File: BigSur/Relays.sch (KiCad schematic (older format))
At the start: 3 parts, among them K1 G5LE-1A-VDDC12, Q3 Q_NPN_BCE

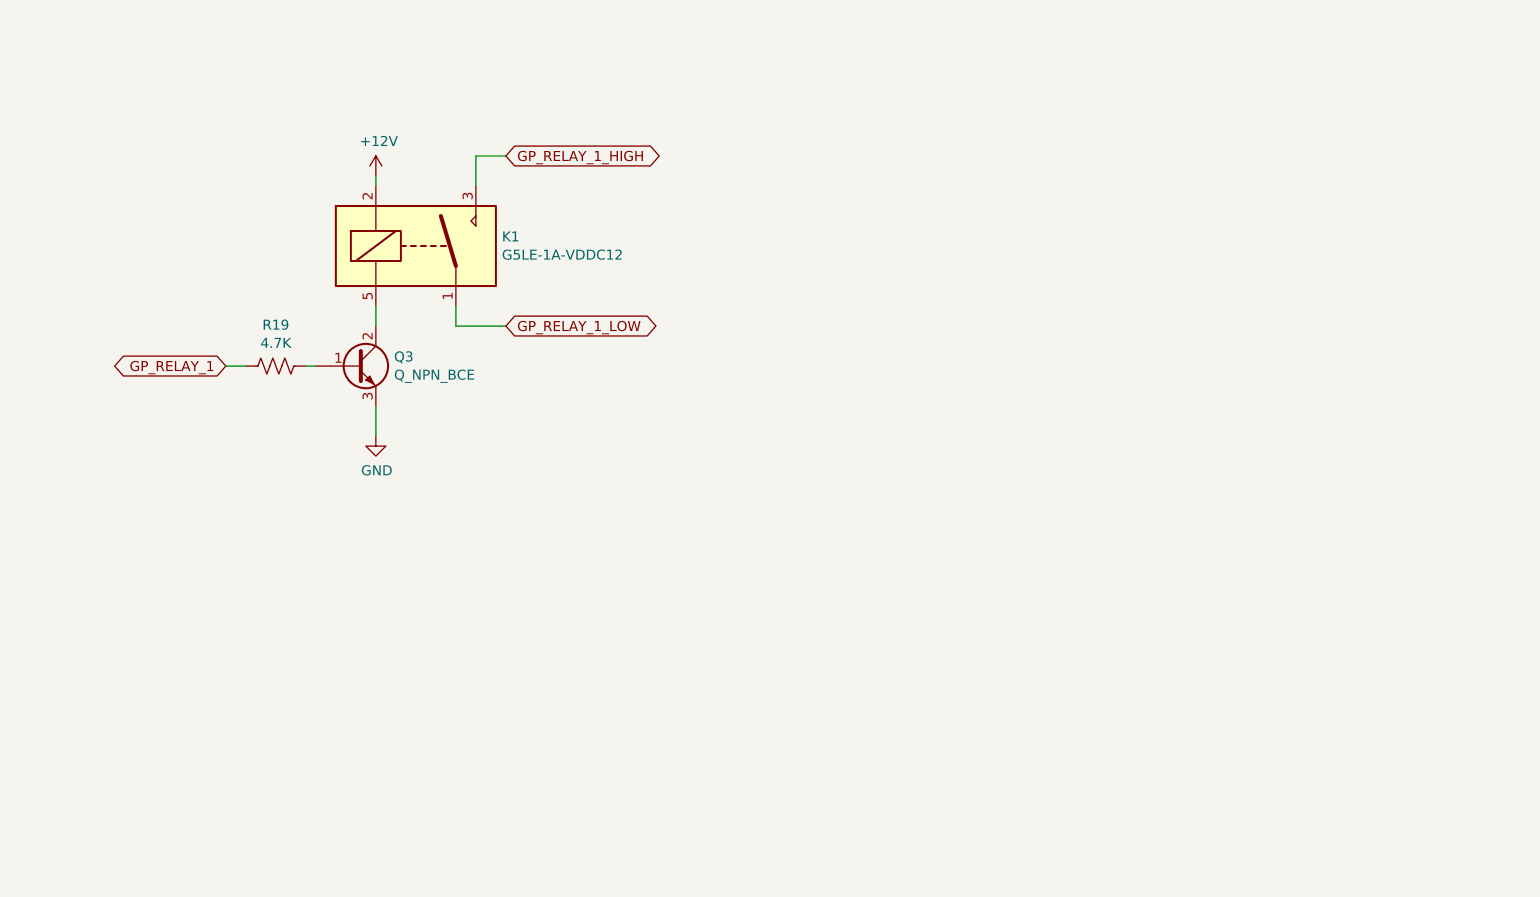
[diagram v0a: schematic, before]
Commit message: Updated test points
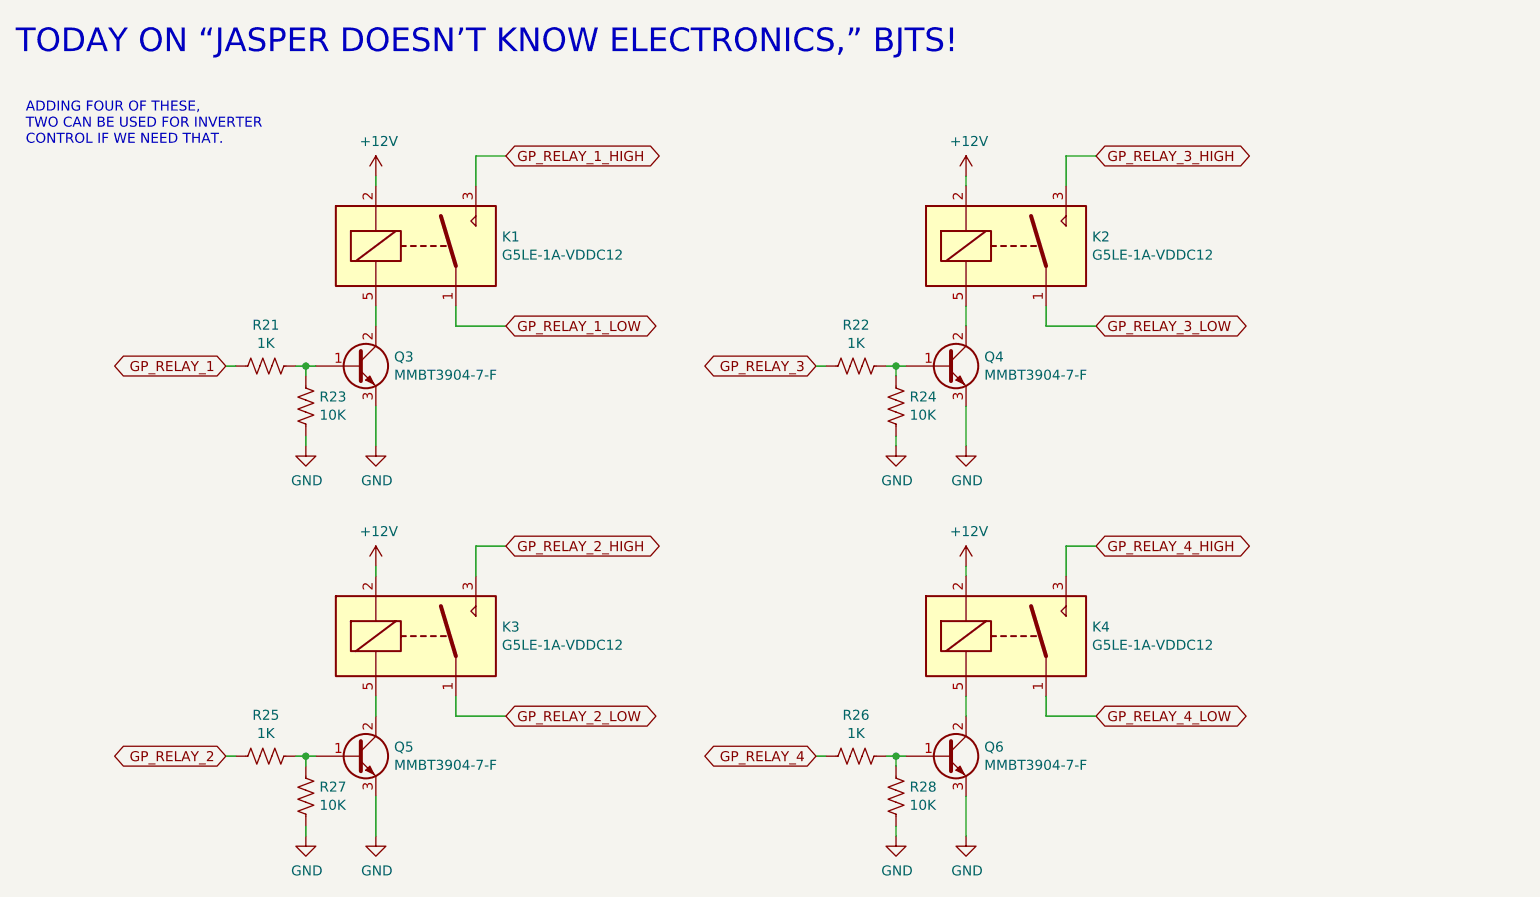
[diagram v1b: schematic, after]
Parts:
- added K2, K3, K4: G5LE-1A-VDDC12, BigSur:OMRON_RELAY_G5LE-1A-VDDC12, symbol BigSurLib:G5LE-1A-VDDC12
- added Q4, Q5, Q6: MMBT3904-7-F, Package_TO_SOT_SMD:SOT-23_Handsoldering, symbol Device:Q_NPN_BCE
- added R22, R25, R26: 1K, Resistor_SMD:R_0603_1608Metric_Pad1.05x0.95mm_HandSolder, symbol Device:R_US
- added R23, R24, R27, R28: 10K, Resistor_SMD:R_0603_1608Metric_Pad1.05x0.95mm_HandSolder, symbol Device:R_US
- Q3: value Q_NPN_BCE -> MMBT3904-7-F; footprint (none) -> Package_TO_SOT_SMD:SOT-23_Handsoldering; Digikey (none) -> https://www.digikey.ca/product-detail/en/diodes-incorporate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
- R21: renamed from R19; value 4.7K -> 1K; footprint (none) -> Resistor_SMD:R_0603_1608Metric_Pad1.05x0.95mm_HandSolder; Digikey (none) -> https://www.digikey.ca/product-detail/en/stackpole-electron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; Part Number (none) -> RMCF0603JJ1K00
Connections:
- net +12V: now also K2.2, K3.2, K4.2
- net GND: now also Q4.3 (E), Q5.3 (E), Q6.3 (E), R23.2, R24.2, R27.2, R28.2
- net at Q3.1 (B), R21.1: now also R23.1
- new net: Q5.1 (B), R25.1, R27.1
- new net: K3.5, Q5.2 (C)
- new net: Q4.1 (B), R22.1, R24.1
- new net: K2.5, Q4.2 (C)
- new net: Q6.1 (B), R26.1, R28.1
- new net: K4.5, Q6.2 (C)
- new net GP_RELAY_2: R25.2
- new net GP_RELAY_2_HIGH: K3.3
- new net GP_RELAY_2_LOW: K3.1
- new net GP_RELAY_3: R22.2
- new net GP_RELAY_3_HIGH: K2.3
- new net GP_RELAY_3_LOW: K2.1
- new net GP_RELAY_4: R26.2
- new net GP_RELAY_4_HIGH: K4.3
- new net GP_RELAY_4_LOW: K4.1
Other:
- note added: "ADDING FOUR OF THESE,\nTWO CAN BE USED FOR INVERTER\nCONTROL IF WE NEED THAT."
- note added: "TODAY ON “JASPER DOESN’T KNOW ELECTRONICS,” BJTS!"
- moved on the sheet: R21

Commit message: Added braking detection, relay flyback, changed current sensors.
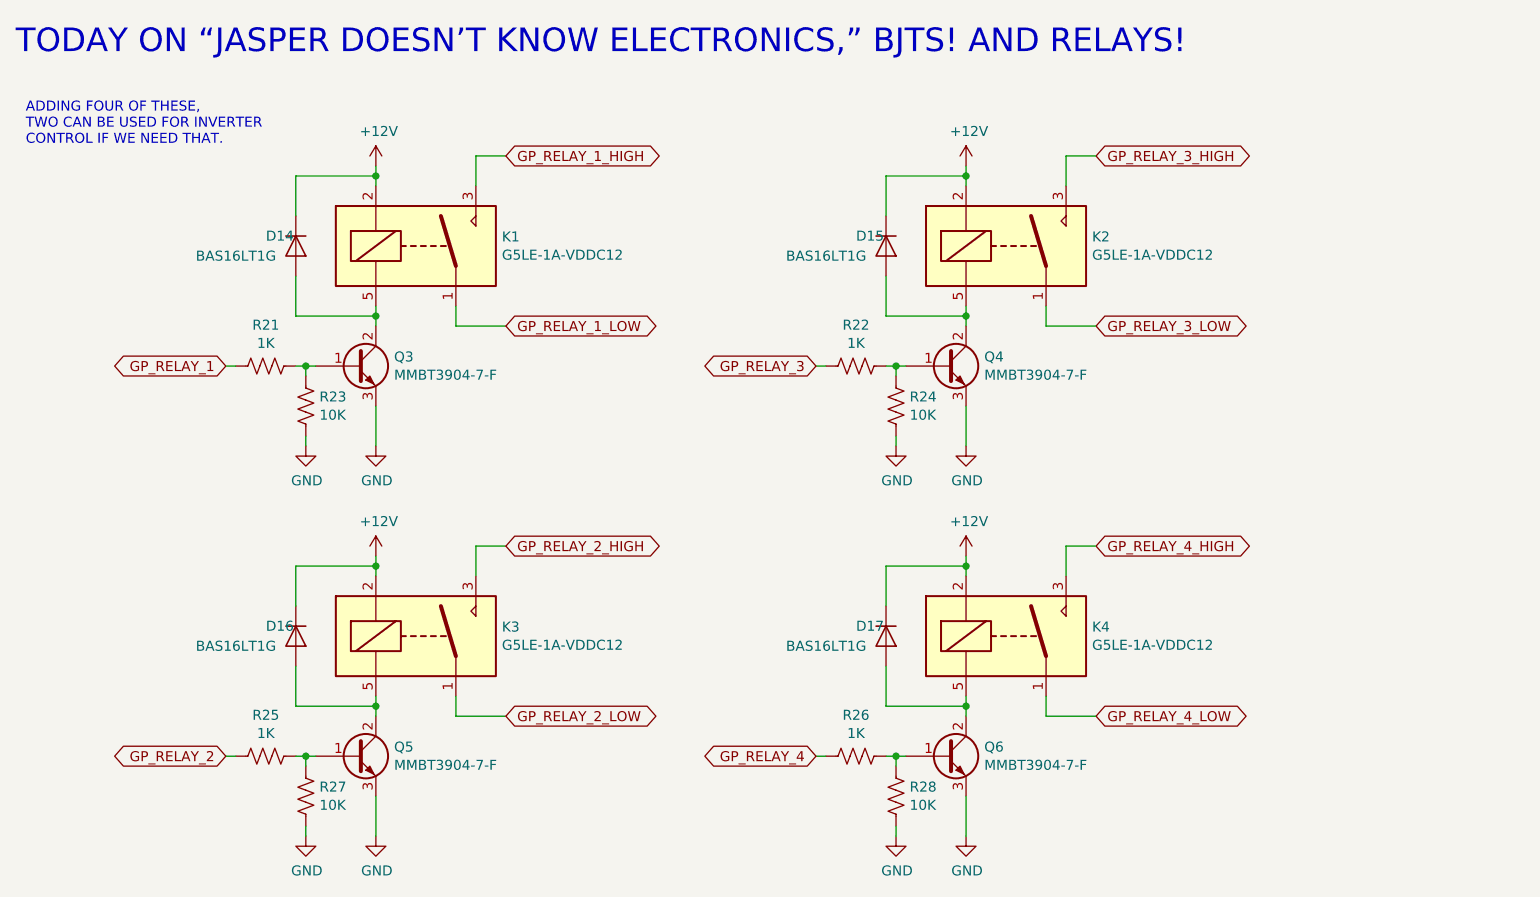
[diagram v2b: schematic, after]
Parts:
- added D14, D15, D16, D17: BAS16LT1G, Package_TO_SOT_SMD:SOT-23_Handsoldering, symbol Device:D
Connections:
- net +12V: now also D14.1 (K), D15.1 (K), D16.1 (K), D17.1 (K)
- net at K3.5, Q5.2 (C): now also D16.2 (A)
- net at K2.5, Q4.2 (C): now also D15.2 (A)
- net at K4.5, Q6.2 (C): now also D17.2 (A)
- net at K1.5, Q3.2 (C): now also D14.2 (A)
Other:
- note added: "TODAY ON “JASPER DOESN’T KNOW ELECTRONICS,” BJTS! AND RELAYS!"
- note removed: "TODAY ON “JASPER DOESN’T KNOW ELECTRONICS,” BJTS!"
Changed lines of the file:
@@
 $EndComp
 Wire Wire Line
-	2400 2000 2400 2100
-Wire Wire Line
-	2400 1350 2400 1400
+	2400 2000 2400 2050
+Wire Wire Line
+	2400 1300 2400 1350
 $Comp
 L power:+12V #PWR064
 U 1 1 5DA90131
-P 2400 1350
-F 0 "#PWR064" H 2400 1200 50  0001 C CNN
-F 1 "+12V" H 2415 1523 50  0000 C CNN
-F 2 "" H 2400 1350 50  0001 C CNN
-F 3 "" H 2400 1350 50  0001 C CNN
-	1    2400 1350
+P 2400 1300
+F 0 "#PWR064" H 2400 1150 50  0001 C CNN
+F 1 "+12V" H 2415 1473 50  0000 C CNN
+F 2 "" H 2400 1300 50  0001 C CNN
+F 3 "" H 2400 1300 50  0001 C CNN
+	1    2400 1300
 	1    0    0    -1
 $EndComp
@@
 GP_RELAY_1_HIGH
 Text Notes 600  750  0    118  ~ 0
-TODAY ON “JASPER DOESN’T KNOW ELECTRONICS,” BJTS!
+TODAY ON “JASPER DOESN’T KNOW ELECTRONICS,” BJTS! AND RELAYS!
 $Comp
 L Device:Q_NPN_BCE Q5
@@
 $EndComp
 Wire Wire Line
-	2400 3950 2400 4050
-Wire Wire Line
-	2400 3300 2400 3350
+	2400 3950 2400 4000
+Wire Wire Line
+	2400 3250 2400 3300
 $Comp
 L power:+12V #PWR070
 U 1 1 5DA0A60C
-P 2400 3300
-F 0 "#PWR070" H 2400 3150 50  0001 C CNN
-F 1 "+12V" H 2415 3473 50  0000 C CNN
-F 2 "" H 2400 3300 50  0001 C CNN
-F 3 "" H 2400 3300 50  0001 C CNN
-	1    2400 3300
+P 2400 3250
+F 0 "#PWR070" H 2400 3100 50  0001 C CNN
+F 1 "+12V" H 2415 3423 50  0000 C CNN
+F 2 "" H 2400 3250 50  0001 C CNN
+F 3 "" H 2400 3250 50  0001 C CNN
+	1    2400 3250
 	1    0    0    -1
 $EndComp
@@
 $EndComp
 Wire Wire Line
-	5350 2000 5350 2100
-Wire Wire Line
-	5350 1350 5350 1400
+	5350 2000 5350 2050
+Wire Wire Line
+	5350 1300 5350 1350
 $Comp
 L power:+12V #PWR065
 U 1 1 5DA0EF32
-P 5350 1350
-F 0 "#PWR065" H 5350 1200 50  0001 C CNN
-F 1 "+12V" H 5365 1523 50  0000 C CNN
-F 2 "" H 5350 1350 50  0001 C CNN
-F 3 "" H 5350 1350 50  0001 C CNN
-	1    5350 1350
+P 5350 1300
+F 0 "#PWR065" H 5350 1150 50  0001 C CNN
+F 1 "+12V" H 5365 1473 50  0000 C CNN
+F 2 "" H 5350 1300 50  0001 C CNN
+F 3 "" H 5350 1300 50  0001 C CNN
+	1    5350 1300
 	1    0    0    -1
 $EndComp
@@
 $EndComp
 Wire Wire Line
-	5350 3950 5350 4050
-Wire Wire Line
-	5350 3300 5350 3350
+	5350 3950 5350 4000
+Wire Wire Line
+	5350 3250 5350 3300
 $Comp
 L power:+12V #PWR071
 U 1 1 5DA0EF72
-P 5350 3300
-F 0 "#PWR071" H 5350 3150 50  0001 C CNN
-F 1 "+12V" H 5365 3473 50  0000 C CNN
-F 2 "" H 5350 3300 50  0001 C CNN
-F 3 "" H 5350 3300 50  0001 C CNN
-	1    5350 3300
+P 5350 3250
+F 0 "#PWR071" H 5350 3100 50  0001 C CNN
+F 1 "+12V" H 5365 3423 50  0000 C CNN
+F 2 "" H 5350 3250 50  0001 C CNN
+F 3 "" H 5350 3250 50  0001 C CNN
+	1    5350 3250
 	1    0    0    -1
 $EndComp
@@
 	0    1    1    0
 $EndComp
+$Comp
+L Device:D D14
+U 1 1 5DC73A46
+P 2000 1700
+F 0 "D14" V 1950 1550 50  0000 L CNN
+F 1 "BAS16LT1G" V 2050 1200 50  0000 L CNN
+F 2 "Package_TO_SOT_SMD:SOT-23_Handsoldering" H 2000 1700 50  0001 C CNN
+F 3 "https://www.onsemi.com/pub/Collateral/BAS16LT1-D.PDF" H 2000 1700 50  0001 C CNN
+F 4 "https://www.digikey.ca/product-detail/en/on-semiconductor/BAS16LT1G/BAS16LT1GOSCT-ND/917796" V 2000 1700 50  0001 C CNN "Digikey"
+	1    2000 1700
+	0    1    1    0
+$EndComp
+Wire Wire Line
+	2400 1350 2000 1350
+Wire Wire Line
+	2000 1350 2000 1550
+Connection ~ 2400 1350
+Wire Wire Line
+	2400 1350 2400 1400
+Wire Wire Line
+	2000 2050 2400 2050
+Wire Wire Line
+	2000 1850 2000 2050
+Connection ~ 2400 2050
+Wire Wire Line
+	2400 2050 2400 2100
+$Comp
+L Device:D D15
+U 1 1 5DC7A8DA
+P 4950 1700
+F 0 "D15" V 4900 1550 50  0000 L CNN
+F 1 "BAS16LT1G" V 5000 1200 50  0000 L CNN
+F 2 "Package_TO_SOT_SMD:SOT-23_Handsoldering" H 4950 1700 50  0001 C CNN
+F 3 "https://www.onsemi.com/pub/Collateral/BAS16LT1-D.PDF" H 4950 1700 50  0001 C CNN
+F 4 "https://www.digikey.ca/product-detail/en/on-semiconductor/BAS16LT1G/BAS16LT1GOSCT-ND/917796" V 4950 1700 50  0001 C CNN "Digikey"
+	1    4950 1700
+	0    1    1    0
+$EndComp
+Wire Wire Line
+	5350 1350 4950 1350
+Wire Wire Line
+	4950 1350 4950 1550
+Wire Wire Line
+	4950 2050 5350 2050
+Wire Wire Line
+	4950 1850 4950 2050
+Connection ~ 5350 1350
+Wire Wire Line
+	5350 1350 5350 1400
+Connection ~ 5350 2050
+Wire Wire Line
+	5350 2050 5350 2100
+$Comp
+L Device:D D16
+U 1 1 5DC7DB2D
+P 2000 3650
+F 0 "D16" V 1950 3500 50  0000 L CNN
+F 1 "BAS16LT1G" V 2050 3150 50  0000 L CNN
+F 2 "Package_TO_SOT_SMD:SOT-23_Handsoldering" H 2000 3650 50  0001 C CNN
+F 3 "https://www.onsemi.com/pub/Collateral/BAS16LT1-D.PDF" H 2000 3650 50  0001 C CNN
+F 4 "https://www.digikey.ca/product-detail/en/on-semiconductor/BAS16LT1G/BAS16LT1GOSCT-ND/917796" V 2000 3650 50  0001 C CNN "Digikey"
+	1    2000 3650
+	0    1    1    0
+$EndComp
+Wire Wire Line
+	2400 3300 2000 3300
+Wire Wire Line
+	2000 3300 2000 3500
+Wire Wire Line
+	2000 4000 2400 4000
+Wire Wire Line
+	2000 3800 2000 4000
+$Comp
+L Device:D D17
+U 1 1 5DC7F716
+P 4950 3650
+F 0 "D17" V 4900 3500 50  0000 L CNN
+F 1 "BAS16LT1G" V 5000 3150 50  0000 L CNN
+F 2 "Package_TO_SOT_SMD:SOT-23_Handsoldering" H 4950 3650 50  0001 C CNN
+F 3 "https://www.onsemi.com/pub/Collateral/BAS16LT1-D.PDF" H 4950 3650 50  0001 C CNN
+F 4 "https://www.digikey.ca/product-detail/en/on-semiconductor/BAS16LT1G/BAS16LT1GOSCT-ND/917796" V 4950 3650 50  0001 C CNN "Digikey"
+	1    4950 3650
+	0    1    1    0
+$EndComp
+Wire Wire Line
+	5350 3300 4950 3300
+Wire Wire Line
+	4950 3300 4950 3500
+Wire Wire Line
+	4950 4000 5350 4000
+Wire Wire Line
+	4950 3800 4950 4000
+Connection ~ 5350 3300
+Wire Wire Line
+	5350 3300 5350 3350
+Connection ~ 5350 4000
+Wire Wire Line
+	5350 4000 5350 4050
+Connection ~ 2400 4000
+Wire Wire Line
+	2400 4000 2400 4050
+Connection ~ 2400 3300
+Wire Wire Line
+	2400 3300 2400 3350
 $EndSCHEMATC
